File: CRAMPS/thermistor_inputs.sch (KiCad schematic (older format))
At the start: 30 parts, among them P301 CONN_4X2, U1001 TL431_SOT23_RMC

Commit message: Schematic updates mostly complete Pending pin assignment which will happen based on PCB layout Updated netlist imported to PCB, but placement not started
Signed-off-by: Charles Steinkuehler <charles@steinkuehler.net>
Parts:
- added JP201: JUMP_MINI, ~, symbol JUMP_MINI
- R1002: value 10k -> 1k
- R1003: value 1k5 -> 2160R 1%
- R1004: value 1k -> 12k4 1%
- R301, R302, R303, R501: value 1k -> 1k 1%
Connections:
- net labels added: ADC_GND, ADC_VDD, AIN3
- net labels removed: +12P, AREF, GND, GNDA
- wire segments 81 -> 83
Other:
- note added: "1.5V Clamp Reference\nDiodes begin to conduct (uA) around 1.775V"
- note added: "Remove jumper to support\n4-wire touch-screen"
- note removed: "Limit at 3.1V"
- moved on the sheet: C301, C302, C303, C501, C502, C503, C504, C505, D1001, D1002, D1003, D1004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

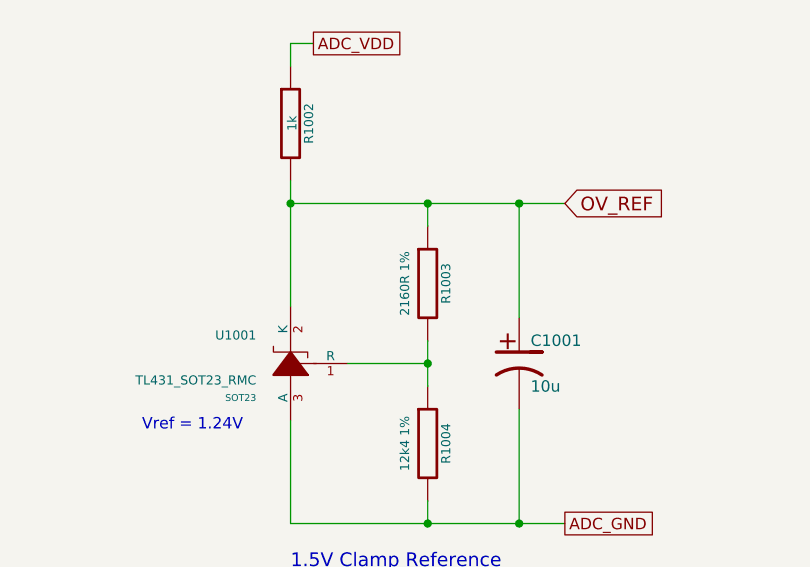
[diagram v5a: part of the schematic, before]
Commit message: Initial BOM files for PCB version 1.0 Added README and ToDo text files
Signed-off-by: Charles Steinkuehler <charles@steinkuehler.net>
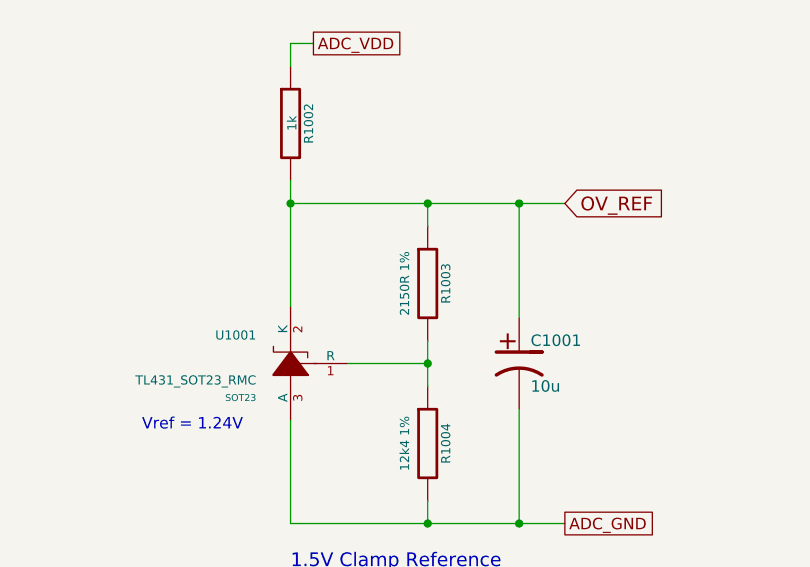
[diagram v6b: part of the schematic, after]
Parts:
- C1001, C301, C302, C303, C501: Mfg (none) -> Taiyo Yuden; PartNo (none) -> LMK212F106ZG-T
- C502, C503, C504, C505: Mfg (none) -> Taiyo Yuden; PartNo (none) -> GMK212BJ104KGHT
- D1001, D1002, D1003, D1004, D1005, D1006, D1007, D1008: Mfg (none) -> Micro Commercial; PartNo (none) -> 1N4148WX-TP
- JP201: Mfg (none) -> Harwin; PartNo (none) -> M20-9990245
- P301: Mfg (none) -> Harwin; PartNo (none) -> M20-9980445
- R1002, R301, R302, R303, R501: Mfg (none) -> KOA; PartNo (none) -> RK73H2ATTD1001F
- R1003: value 2160R 1% -> 2150R 1%; Mfg (none) -> KOA; PartNo (none) -> RK73H2ATTD2151F
- R1004: Mfg (none) -> KOA; PartNo (none) -> RK73H2ATTD1002F
- R502, R503, R504, R505: Mfg (none) -> KOA; PartNo (none) -> RK73H2ATTD4701F
- U1001: Mfg (none) -> TI; PartNo (none) -> TLV431CDBZR
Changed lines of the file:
@@
 Sheet 10 10
 Title "CRAMPS (Cape-RAMPS for BeagleBone)"
-Date "9 feb 2014"
+Date "11 feb 2014"
 Rev "v1.0"
 Comp ""
@@
 F 2 "" H 4350 1600 60  0001 C CNN
 F 3 "" H 4350 1600 60  0001 C CNN
+F 4 "KOA" H 6250 6550 60  0001 C CNN "Mfg"
+F 5 "RK73H2ATTD4701F" H 6250 6550 60  0001 C CNN "PartNo"
 	1    4350 1600
 	0    -1   -1   0
@@
 F 2 "" H 5200 1900 60  0001 C CNN
 F 3 "" H 5200 1900 60  0001 C CNN
+F 4 "Taiyo Yuden" H 6250 6550 60  0001 C CNN "Mfg"
+F 5 "GMK212BJ104KGHT" H 6250 6550 60  0001 C CNN "PartNo"
 	1    5200 1900
 	1    0    0    -1
@@
 F 2 "" H 4350 3200 60  0001 C CNN
 F 3 "" H 4350 3200 60  0001 C CNN
+F 4 "KOA" H 6250 6550 60  0001 C CNN "Mfg"
+F 5 "RK73H2ATTD4701F" H 6250 6550 60  0001 C CNN "PartNo"
 	1    4350 3200
 	0    -1   -1   0
@@
 F 2 "" H 5200 3500 60  0001 C CNN
 F 3 "" H 5200 3500 60  0001 C CNN
+F 4 "Taiyo Yuden" H 6250 6550 60  0001 C CNN "Mfg"
+F 5 "GMK212BJ104KGHT" H 6250 6550 60  0001 C CNN "PartNo"
 	1    5200 3500
 	1    0    0    -1
@@
 F 2 "" H 5200 5100 60  0001 C CNN
 F 3 "" H 5200 5100 60  0001 C CNN
+F 4 "Taiyo Yuden" H 6250 6550 60  0001 C CNN "Mfg"
+F 5 "GMK212BJ104KGHT" H 6250 6550 60  0001 C CNN "PartNo"
 	1    5200 5100
 	1    0    0    -1
@@
 F 2 "" H 4350 4800 60  0001 C CNN
 F 3 "" H 4350 4800 60  0001 C CNN
+F 4 "KOA" H 6250 6550 60  0001 C CNN "Mfg"
+F 5 "RK73H2ATTD4701F" H 6250 6550 60  0001 C CNN "PartNo"
 	1    4350 4800
 	0    -1   -1   0
@@
 F 2 "" H 4350 6400 60  0001 C CNN
 F 3 "" H 4350 6400 60  0001 C CNN
+F 4 "KOA" H 6250 6550 60  0001 C CNN "Mfg"
+F 5 "RK73H2ATTD4701F" H 6250 6550 60  0001 C CNN "PartNo"
 	1    4350 6400
 	0    -1   -1   0
@@
 F 2 "" H 5200 6700 60  0001 C CNN
 F 3 "" H 5200 6700 60  0001 C CNN
+F 4 "Taiyo Yuden" H 6250 6550 60  0001 C CNN "Mfg"
+F 5 "GMK212BJ104KGHT" H 6250 6550 60  0001 C CNN "PartNo"
 	1    5200 6700
 	1    0    0    -1
@@
 F 2 "" H 3900 6050 60  0001 C CNN
 F 3 "" H 3900 6050 60  0001 C CNN
+F 4 "KOA" H 6250 6550 60  0001 C CNN "Mfg"
+F 5 "RK73H2ATTD1001F" H 6250 6550 60  0001 C CNN "PartNo"
 	1    3900 6050
 	1    0    0    -1
@@
 F 2 "" H 5600 6700 60  0001 C CNN
 F 3 "" H 5600 6700 60  0001 C CNN
+F 4 "Taiyo Yuden" H 6250 6550 60  0001 C CNN "Mfg"
+F 5 "LMK212F106ZG-T" H 6250 6550 60  0001 C CNN "PartNo"
 	1    5600 6700
 	1    0    0    -1
@@
 F 2 "" H 2300 2550 60  0001 C CNN
 F 3 "" H 2300 2550 60  0001 C CNN
+F 4 "Harwin" H 6250 6550 60  0001 C CNN "Mfg"
+F 5 "M20-9980445" H 6250 6550 60  0001 C CNN "PartNo"
 	1    2300 2550
 	1    0    0    -1
@@
 F 2 "" H 5600 5100 60  0001 C CNN
 F 3 "" H 5600 5100 60  0001 C CNN
+F 4 "Taiyo Yuden" H 6250 6550 60  0001 C CNN "Mfg"
+F 5 "LMK212F106ZG-T" H 6250 6550 60  0001 C CNN "PartNo"
 	1    5600 5100
 	1    0    0    -1
@@
 F 2 "" H 3900 4450 60  0001 C CNN
 F 3 "" H 3900 4450 60  0001 C CNN
+F 4 "KOA" H 6250 6550 60  0001 C CNN "Mfg"
+F 5 "RK73H2ATTD1001F" H 6250 6550 60  0001 C CNN "PartNo"
 	1    3900 4450
 	1    0    0    -1
@@
 F 2 "" H 3900 2850 60  0001 C CNN
 F 3 "" H 3900 2850 60  0001 C CNN
+F 4 "KOA" H 6250 6550 60  0001 C CNN "Mfg"
+F 5 "RK73H2ATTD1001F" H 6250 6550 60  0001 C CNN "PartNo"
 	1    3900 2850
 	1    0    0    -1
@@
 F 2 "" H 5600 3500 60  0001 C CNN
 F 3 "" H 5600 3500 60  0001 C CNN
+F 4 "Taiyo Yuden" H 6250 6550 60  0001 C CNN "Mfg"
+F 5 "LMK212F106ZG-T" H 6250 6550 60  0001 C CNN "PartNo"
 	1    5600 3500
 	1    0    0    -1
@@
 F 2 "" H 5600 1900 60  0001 C CNN
 F 3 "" H 5600 1900 60  0001 C CNN
+F 4 "Taiyo Yuden" H 6250 6550 60  0001 C CNN "Mfg"
+F 5 "LMK212F106ZG-T" H 6250 6550 60  0001 C CNN "PartNo"
 	1    5600 1900
 	1    0    0    -1
@@
 F 2 "" H 3900 1250 60  0001 C CNN
 F 3 "" H 3900 1250 60  0001 C CNN
+F 4 "KOA" H 6250 6550 60  0001 C CNN "Mfg"
+F 5 "RK73H2ATTD1001F" H 6250 6550 60  0001 C CNN "PartNo"
 	1    3900 1250
 	1    0    0    -1
@@
 F 2 "~" H 4800 1900 60  0000 C CNN
 F 3 "~" H 4800 1900 60  0000 C CNN
+F 4 "Micro Commercial" H 6250 6550 60  0001 C CNN "Mfg"
+F 5 "1N4148WX-TP" H 6250 6550 60  0001 C CNN "PartNo"
 	1    4800 1900
 	0    -1   -1   0
@@
 F 2 "~" H 4800 1300 60  0000 C CNN
 F 3 "~" H 4800 1300 60  0000 C CNN
+F 4 "Micro Commercial" H 6250 6550 60  0001 C CNN "Mfg"
+F 5 "1N4148WX-TP" H 6250 6550 60  0001 C CNN "PartNo"
 	1    4800 1300
 	0    -1   -1   0
@@
 F 2 "~" V 8530 2350 30  0000 C CNN
 F 3 "~" H 8600 2350 30  0000 C CNN
+F 4 "KOA" H 6250 6550 60  0001 C CNN "Mfg"
+F 5 "RK73H2ATTD1001F" H 6250 6550 60  0001 C CNN "PartNo"
 	1    8600 2350
 	1    0    0    -1
@@
 F 2 "~" V 9130 3750 30  0000 C CNN
 F 3 "~" H 9200 3750 30  0000 C CNN
+F 4 "KOA" H 6250 6550 60  0001 C CNN "Mfg"
+F 5 "RK73H2ATTD1002F" H 6250 6550 60  0001 C CNN "PartNo"
 	1    9200 3750
 	1    0    0    -1
@@
 P 9200 3050
 F 0 "R1003" V 9280 3050 40  0000 C CNN
-F 1 "2160R 1%" V 9100 3050 40  0000 C CNN
+F 1 "2150R 1%" V 9100 3050 40  0000 C CNN
 F 2 "~" V 9130 3050 30  0000 C CNN
 F 3 "~" H 9200 3050 30  0000 C CNN
+F 4 "KOA" H 6250 6550 60  0001 C CNN "Mfg"
+F 5 "RK73H2ATTD2151F" H 6250 6550 60  0001 C CNN "PartNo"
 	1    9200 3050
 	1    0    0    -1
@@
 F 2 "~" H 9600 3400 60  0000 C CNN
 F 3 "~" H 9600 3400 60  0000 C CNN
+F 4 "Taiyo Yuden" H 6250 6550 60  0001 C CNN "Mfg"
+F 5 "LMK212F106ZG-T" H 6250 6550 60  0001 C CNN "PartNo"
 	1    9600 3400
 	1    0    0    -1
@@
 F 2 "~" H 4800 2900 60  0000 C CNN
 F 3 "~" H 4800 2900 60  0000 C CNN
+F 4 "Micro Commercial" H 6250 6550 60  0001 C CNN "Mfg"
+F 5 "1N4148WX-TP" H 6250 6550 60  0001 C CNN "PartNo"
 	1    4800 2900
 	0    -1   -1   0
@@
 F 2 "~" H 4800 3500 60  0000 C CNN
 F 3 "~" H 4800 3500 60  0000 C CNN
+F 4 "Micro Commercial" H 6250 6550 60  0001 C CNN "Mfg"
+F 5 "1N4148WX-TP" H 6250 6550 60  0001 C CNN "PartNo"
 	1    4800 3500
 	0    -1   -1   0
@@
 F 2 "~" H 4800 5100 60  0000 C CNN
 F 3 "~" H 4800 5100 60  0000 C CNN
+F 4 "Micro Commercial" H 6250 6550 60  0001 C CNN "Mfg"
+F 5 "1N4148WX-TP" H 6250 6550 60  0001 C CNN "PartNo"
 	1    4800 5100
 	0    -1   -1   0
@@
 F 2 "~" H 4800 4500 60  0000 C CNN
 F 3 "~" H 4800 4500 60  0000 C CNN
+F 4 "Micro Commercial" H 6250 6550 60  0001 C CNN "Mfg"
+F 5 "1N4148WX-TP" H 6250 6550 60  0001 C CNN "PartNo"
 	1    4800 4500
 	0    -1   -1   0
@@
 F 2 "~" H 4800 6100 60  0000 C CNN
 F 3 "~" H 4800 6100 60  0000 C CNN
+F 4 "Micro Commercial" H 6250 6550 60  0001 C CNN "Mfg"
+F 5 "1N4148WX-TP" H 6250 6550 60  0001 C CNN "PartNo"
 	1    4800 6100
 	0    -1   -1   0
@@
 F 2 "~" H 4800 6700 60  0000 C CNN
 F 3 "~" H 4800 6700 60  0000 C CNN
+F 4 "Micro Commercial" H 6250 6550 60  0001 C CNN "Mfg"
+F 5 "1N4148WX-TP" H 6250 6550 60  0001 C CNN "PartNo"
 	1    4800 6700
 	0    -1   -1   0
@@
 F 2 "SOT23" H 8750 3250 30  0000 L CNN
 F 3 "~" H 8600 3400 60  0000 C CNN
+F 4 "TI" H 6250 6550 60  0001 C CNN "Mfg"
+F 5 "TLV431CDBZR" H 6250 6550 60  0001 C CNN "PartNo"
 	1    8600 3400
 	-1   0    0    -1
@@
 F 2 "~" H 5950 6100 60  0000 C CNN
 F 3 "~" H 5950 6100 60  0000 C CNN
+F 4 "Harwin" H 6250 6550 60  0001 C CNN "Mfg"
+F 5 "M20-9990245" H 6250 6550 60  0001 C CNN "PartNo"
 	1    5950 6100
 	1    0    0    -1

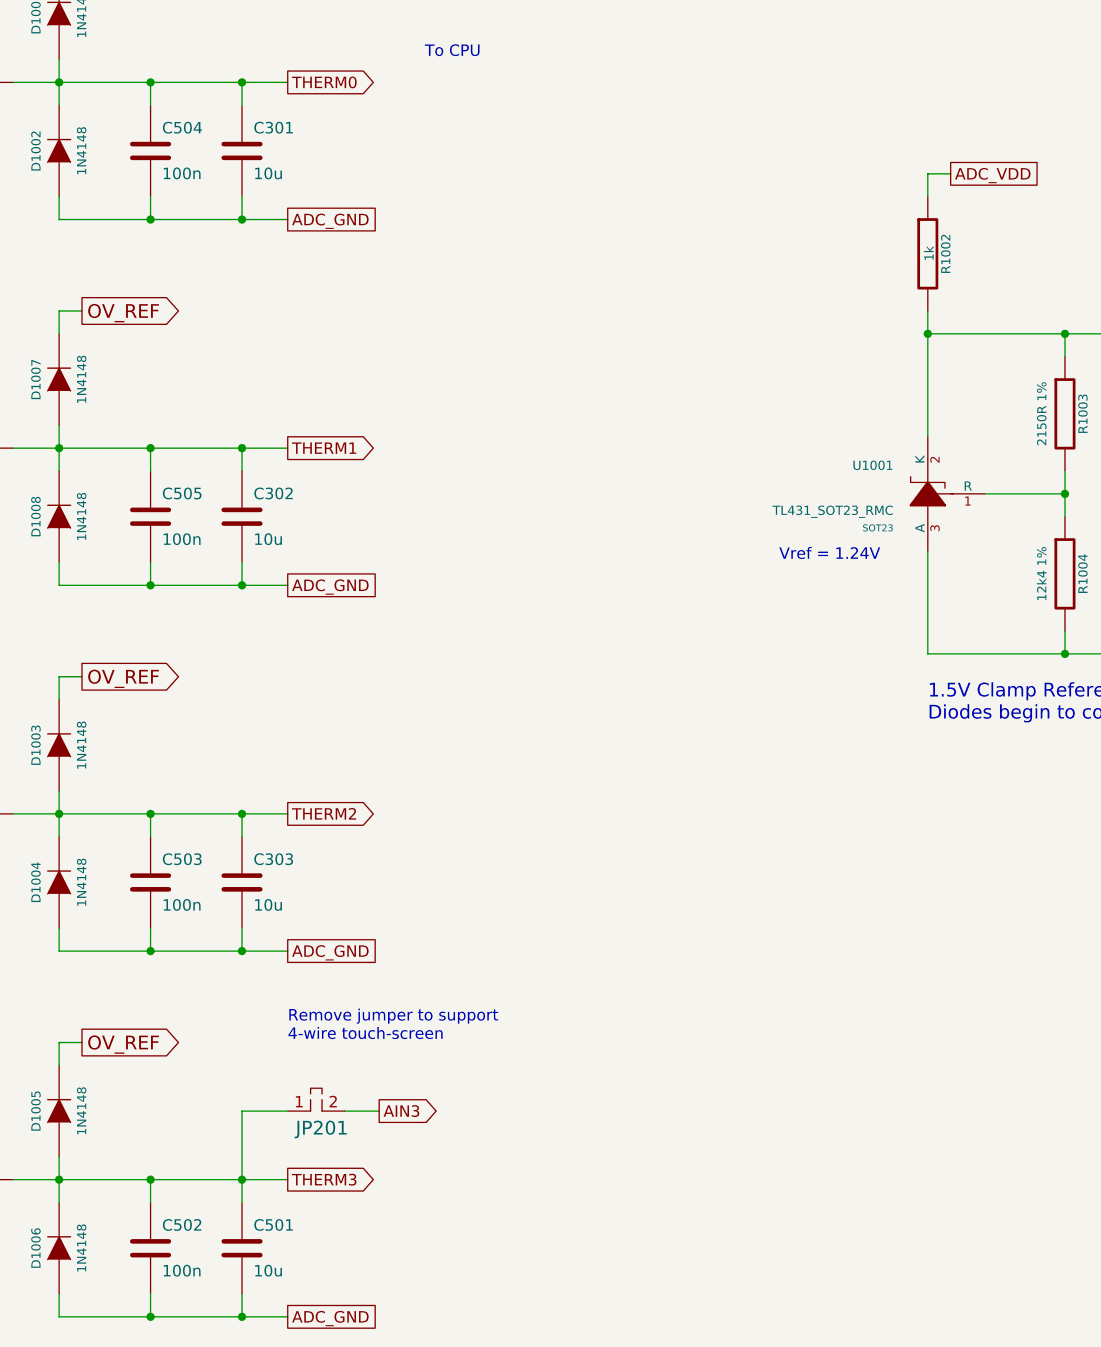
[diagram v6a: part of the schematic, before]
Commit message: BOM Updates Fixed incorrect Molex part number Added Stackpole resistor part numbers Switched to value-sorted BOM export from KiCAD Modified some attribute fields to get same-value parts to list on a single BOM line
Signed-off-by: Charles Steinkuehler <charles@steinkuehler.net>
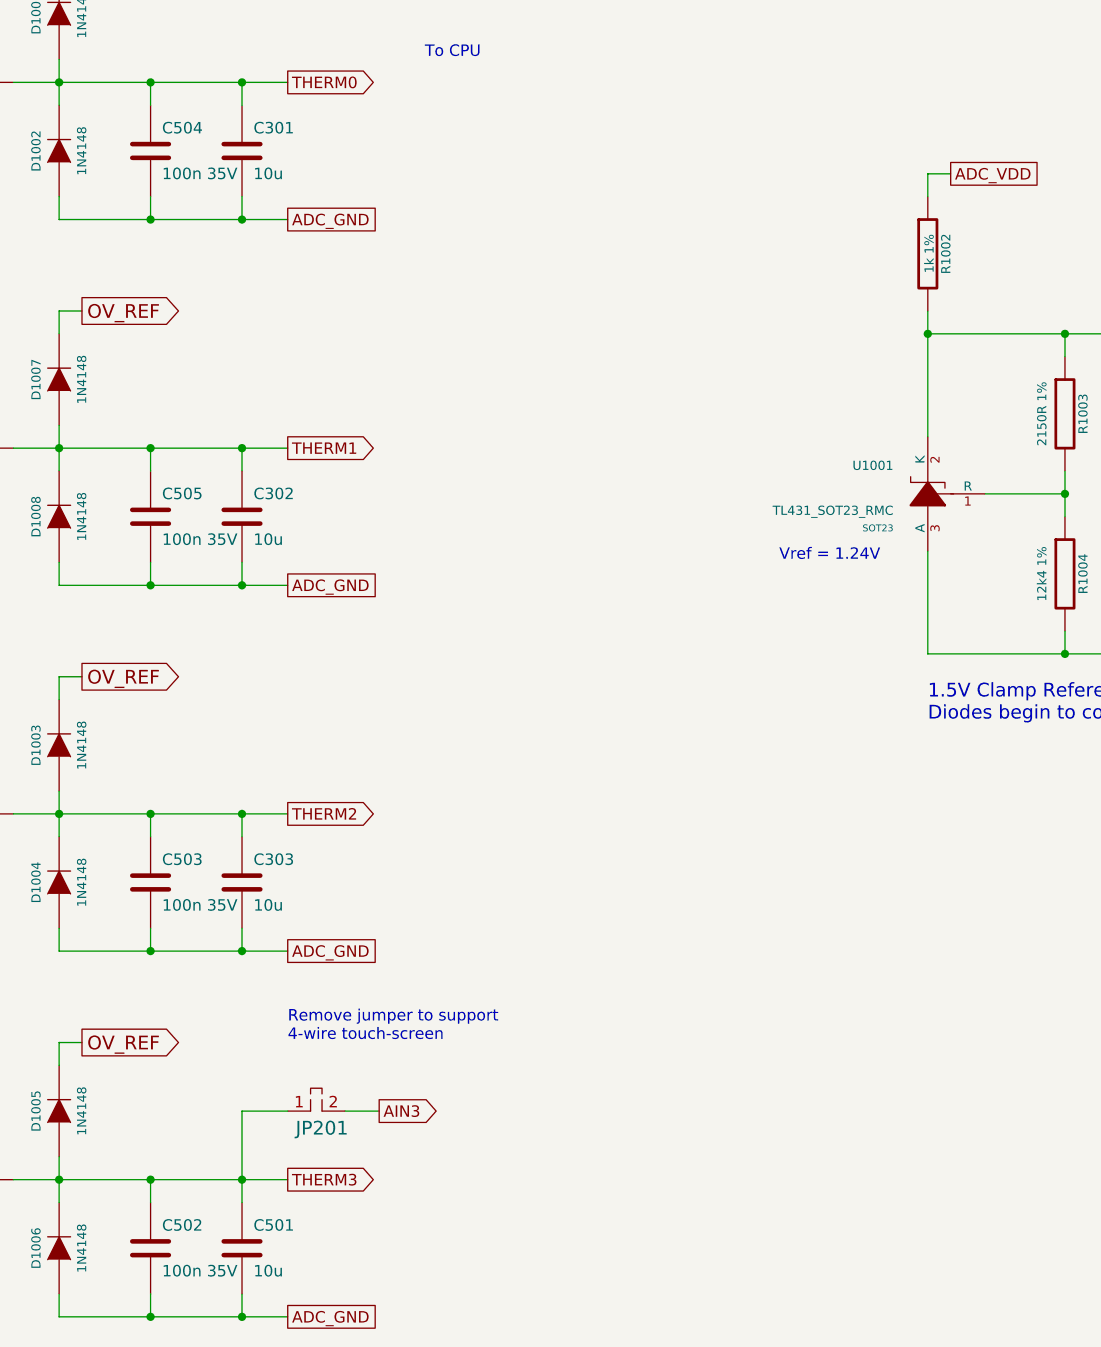
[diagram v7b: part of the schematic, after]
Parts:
- C1001: footprint ~ -> (none)
- C502, C503, C504, C505: value 100n -> 100n 35V
- R1002: value 1k -> 1k 1%; footprint ~ -> (none); AltMfg (none) -> KOA; AltPartNo (none) -> RK73H2ATTD1001F; Mfg KOA -> Stackpole; PartNo RK73H2ATTD1001F -> RMCF0805FT1K00
- R1003: AltMfg (none) -> KOA; AltPartNo (none) -> RK73H2ATTD2151F; Mfg KOA -> Stackpole; PartNo RK73H2ATTD2151F -> RMCF0805FT2K15
- R1004: AltMfg (none) -> KOA; AltPartNo (none) -> RK73H2ATTD1242F; Mfg KOA -> Stackpole; PartNo RK73H2ATTD1002F -> RMCF0805FT12K4
- R301, R302, R303, R501: AltMfg (none) -> KOA; AltPartNo (none) -> RK73H2ATTD1001F; Mfg KOA -> Stackpole; PartNo RK73H2ATTD1001F -> RMCF0805FT1K00
- R502, R503, R504, R505: AltMfg (none) -> KOA; AltPartNo (none) -> RK73H2ATTD4701F; Mfg KOA -> Stackpole; PartNo RK73H2ATTD4701F -> RMCF0805FT4K70
